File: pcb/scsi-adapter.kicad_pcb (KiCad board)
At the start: 4 copper layers, 120 x 90 mm, 404 parts, among them J101 Bench 5V, J201 TERMPWR jumper, J301 IDC50 box header, J302 HD50 female R/A, J303 2x17 box header, J401 TC2030-IDC, J501 TF PUSH, J601 USB-C (HRO TYPE-C-31-M-12), Q1001 FDV301N, Q1101 FDV301N, Q1201 FDV301N, Q1301 FDV301N, Q1401 FDV301N, Q1501 FDV301N, Q1601 FDV301N, Q1701 FDV301N, Q1801 FDV301N, Q1901 FDV301N, Q2001 FDV301N, Q201 2N7002, Q2101 FDV301N, Q2301 FDV301N, Q901 FDV301N, SW301 DIP 2-pos, SW401 BOOTSEL, SW402 RUN, U1001 74LVC1G17GW, U101 TPS259470ARPWR, U102 TPS2116DRLR, U103 TPS73701DCQR, U104 TPS73701DCQR, U1101 74LVC1G17GW, U1201 74LVC1G17GW, U1301 74LVC1G17GW, U1401 74LVC1G17GW, U1501 74LVC1G17GW, U1601 74LVC1G17GW, U1701 74LVC1G17GW, U1801 74LVC1G17GW, U1901 74LVC1G17GW, U2001 74LVC1G17GW, U201 TPS259470ARPWR, U202 LM393DR2G, U203 CJ431, U2101 74LVC1G17GW, U2201 74LVC1G17GW, U2301 74LVC1G17GW, U2401 74LVC1G17GW, U2501 74LVC1G17GW, U2601 74LVC1G17GW, U301 SN74LVTH245APWR, U302 SN74LVTH245APWR, U303 SN74LVTH245APWR, U401 RP2350B, U402 W25Q128JVSIQ, U403 APS6404L-3SQR-SN, U501 TCA9555PWR, U601 CH334P, U701 FT232HL, U702 93LC56BT-I/OT, U901 74LVC1G17GW, Y401 12MHz ABM8-272-T3, Y601 12MHz ABM8-272-T3, Y701 12MHz ABM8-272-T3

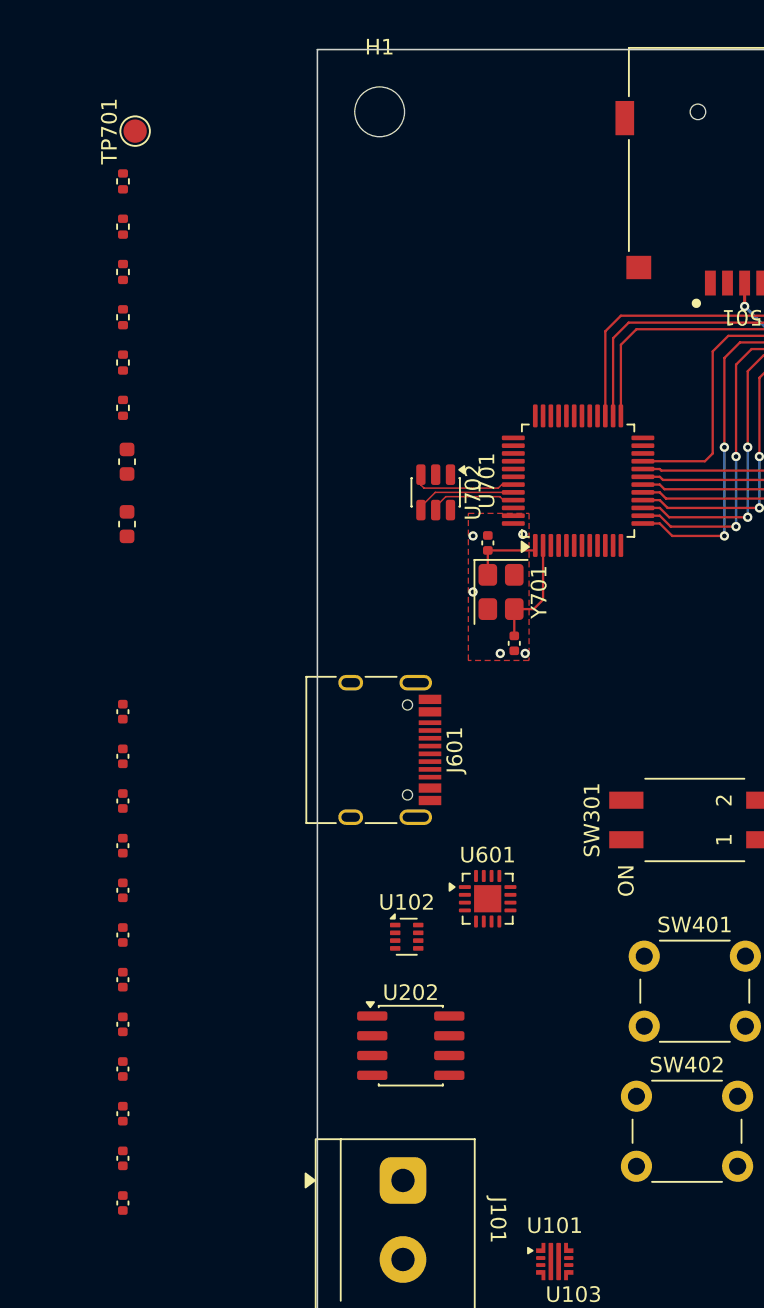
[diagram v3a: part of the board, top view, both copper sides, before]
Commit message: ft232h passives routing
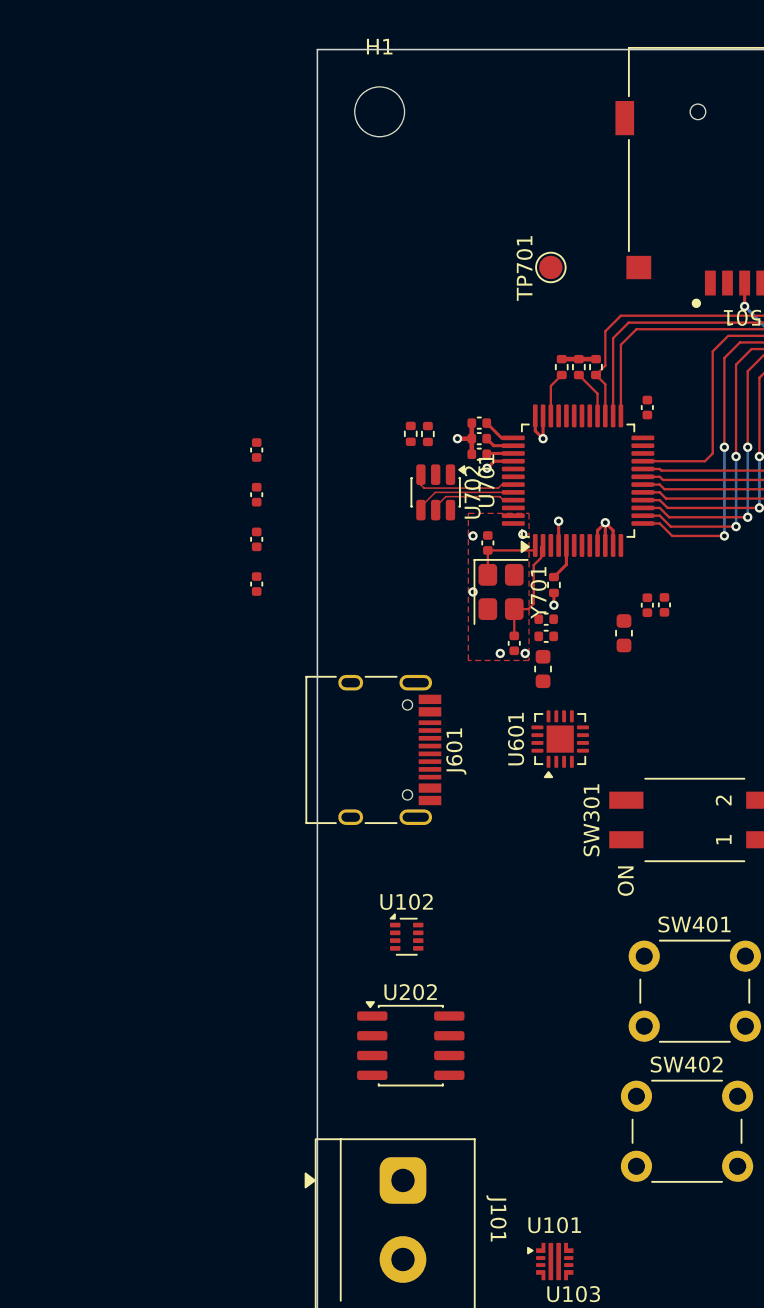
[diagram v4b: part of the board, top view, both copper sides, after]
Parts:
- moved C707 52.0 mm to (121.2, 53.0)
- moved C705 40.7 mm to (96.1, 58.6)
- moved C706 40.7 mm to (96.1, 55.7)
- moved C703 40.7 mm to (96.1, 64.3)
- moved C704 40.7 mm to (96.1, 61.5)
- moved C710 39.3 mm to (122.3, 65.7)
- moved C711 37.1 mm to (121.2, 65.7)
- moved C708 35.0 mm to (114.7, 67.7), turned to 0 degrees
- moved C709 33.9 mm to (114.7, 66.6), turned to 0 degrees
- moved FB702 33.8 mm to (119.7, 67.5)
- moved C712 33.4 mm to (110.4, 54.0), turned to 180 degrees
- moved R705 31.7 mm to (117.9, 50.4), turned to -90 degrees
- moved R706 31.6 mm to (116.8, 50.4), turned to -90 degrees
- moved C713 30.7 mm to (110.4, 55.0), turned to 180 degrees
- moved R701 29.9 mm to (115.2, 64.4), turned to -90 degrees
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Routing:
- net GND: track 17.9 -> 31.1 mm, vias 39 -> 44
- net FT232H_3V3: track 0.00 -> 3.93 mm
- net /ft232h/FT232H_SIWU_N: track 0.00 -> 3.12 mm
- net /FT232H_RESET_INVERTED: track 0.00 -> 2.92 mm
- net /ft232h/FT232H_REF: track 0.00 -> 2.36 mm
- net /ft232h/FT232H_VCCA: track 0.00 -> 2.10 mm
- net /ft232h/FT232H_VCORE: track 0.00 -> 1.89 mm
- net +5V_SYS: track 0.00 -> 1.87 mm, vias 0 -> 1

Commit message: ft232h fully routed
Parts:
- moved R429 183.3 mm to (143.1, 56.8), turned to -135 degrees
- moved R428 182.4 mm to (142.3, 56.0), turned to 45 degrees
- moved C424 135.7 mm to (143.9, 57.6), turned to -135 degrees
- moved C717 87.0 mm to (114.6, 50.4), turned to 90 degrees
- moved C701 74.9 mm to (110.0, 56.6), turned to -90 degrees
- moved C702 74.7 mm to (111.0, 56.6), turned to -90 degrees
- moved C705 25.4 mm to (121.2, 62.3), turned to 0 degrees
- moved C703 17.6 mm to (113.3, 68.3), turned to -90 degrees
- moved C706 14.7 mm to (110.4, 59.3), turned to 180 degrees
- moved C704 11.7 mm to (107.8, 61.3), turned to -90 degrees
- moved FB701 4.42 mm to (114.1, 65.4), turned to 0 degrees
- moved FB702 3.79 mm to (118.9, 63.8), turned to 180 degrees
- moved C710 3.40 mm to (118.9, 65.5), turned to -90 degrees
- moved C711 3.31 mm to (117.9, 65.5), turned to -90 degrees
- moved C716 1.45 mm to (111.3, 67.5)
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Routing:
- net FT232H_3V3: track 3.93 -> 79.2 mm, vias 0 -> 5
- net /rp2350/PSRAM_CE_INVERTED: track 2.08 -> 30.8 mm, vias 0 -> 2
- net GND: track 31.1 -> 55.7 mm, vias 44 -> 50
- net /USB_FT_D-: track 0.00 -> 15.2 mm
- net /usb-hub/USB_D-: track 0.00 -> 13.6 mm
- net /usb-hub/USB_D+: track 0.00 -> 13.6 mm
- net /USB_FT_D+: track 0.00 -> 12.1 mm, vias 0 -> 2
- net /rp2350/TERMPWR_SENSE: track 0.00 -> 7.87 mm
- net /ft232h/FT232H_VPHY: track 0.00 -> 5.99 mm
- net /ft232h/FT232H_VPLL: track 0.00 -> 4.50 mm
- net /ft232h/FT232H_EEPROM_DO: track 0.00 -> 3.02 mm
- net /ft232h/FT232H_EEDATA: track 6.78 -> 9.71 mm
- net +5V_SYS: track 1.87 -> 3.63 mm
- net +3V3: track 57.9 -> 56.5 mm, vias 15 -> 14
- net /ft232h/FT232H_XCSI: track 4.94 -> 6.38 mm
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
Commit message: start routing scsi
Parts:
- moved R312 254.2 mm to (156.1, 90.2), turned to 135 degrees
- moved Q1101 253.1 mm to (241.6, 72.3), turned to -45 degrees
- moved R318 252.9 mm to (175.3, 90.5), turned to 135 degrees
- moved R311 252.3 mm to (155.4, 90.9), turned to 135 degrees
- moved R317 250.9 mm to (174.6, 91.1), turned to 135 degrees
- moved R310 244.9 mm to (156.2, 97.4), turned to 135 degrees
- moved R316 243.6 mm to (175.2, 97.8), turned to 135 degrees
- moved R309 242.9 mm to (155.5, 98.1), turned to 135 degrees
- moved R315 241.7 mm to (174.5, 98.4), turned to 135 degrees
- moved R320 239.9 mm to (185.3, 104.1), turned to 135 degrees
- moved R319 237.9 mm to (184.7, 104.8), turned to 135 degrees
- moved R308 235.7 mm to (156.1, 104.7), turned to 135 degrees
- moved R314 234.1 mm to (175.3, 105.3), turned to 135 degrees
- moved R307 233.7 mm to (155.4, 105.4), turned to 135 degrees
- moved R313 232.1 mm to (174.6, 105.9), turned to 135 degrees
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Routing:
- net GND: track 55.7 -> 128.5 mm, vias 50 -> 101
- net +3V3: track 56.5 -> 91.0 mm, vias 14 -> 32
- net /SEL_GATE: track 0.00 -> 22.2 mm
- net /RST_GATE: track 0.00 -> 21.9 mm
- net /ACK_GATE: track 0.00 -> 21.4 mm
- net /BSY_GATE: track 0.00 -> 21.1 mm
- net /LOGIC_ANALYZER_MARKER1: track 16.1 -> 0.00 mm
- net /scsi/~{RST}: track 0.00 -> 5.85 mm
- net /scsi/~{DB0}: track 0.00 -> 5.85 mm
- net /scsi/~{DB7}: track 0.00 -> 5.84 mm
- net /scsi/~{DB2}: track 0.00 -> 5.84 mm
- net /scsi/~{DB1}: track 0.00 -> 5.84 mm
- net /scsi/~{DBP}: track 0.00 -> 5.84 mm
- net /scsi/~{DB4}: track 0.00 -> 5.84 mm
- net /scsi/~{ACK}: track 0.00 -> 5.84 mm
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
